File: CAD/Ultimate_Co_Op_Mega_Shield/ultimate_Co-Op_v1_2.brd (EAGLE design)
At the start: 78.4 x 53.3 mm, 134 parts

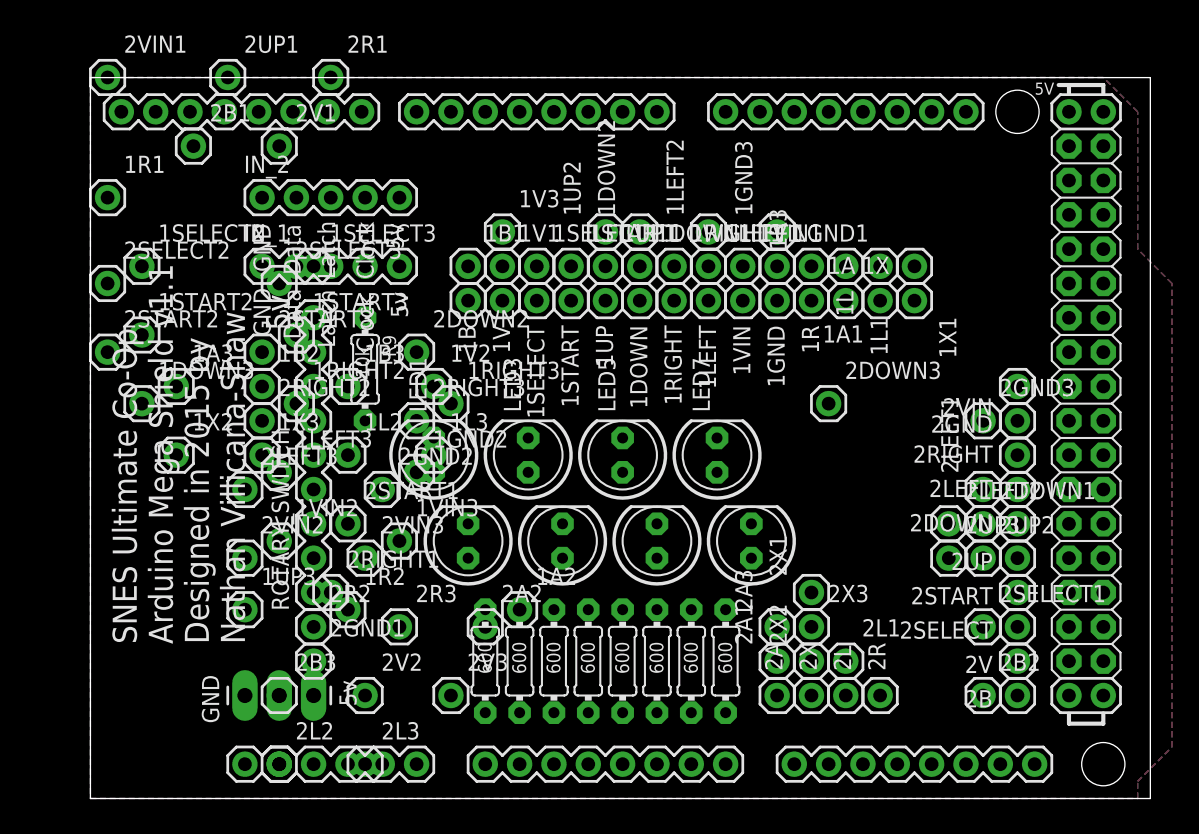
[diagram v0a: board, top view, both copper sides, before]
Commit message: a few minor changes to the board, now has one rotaty and one switch
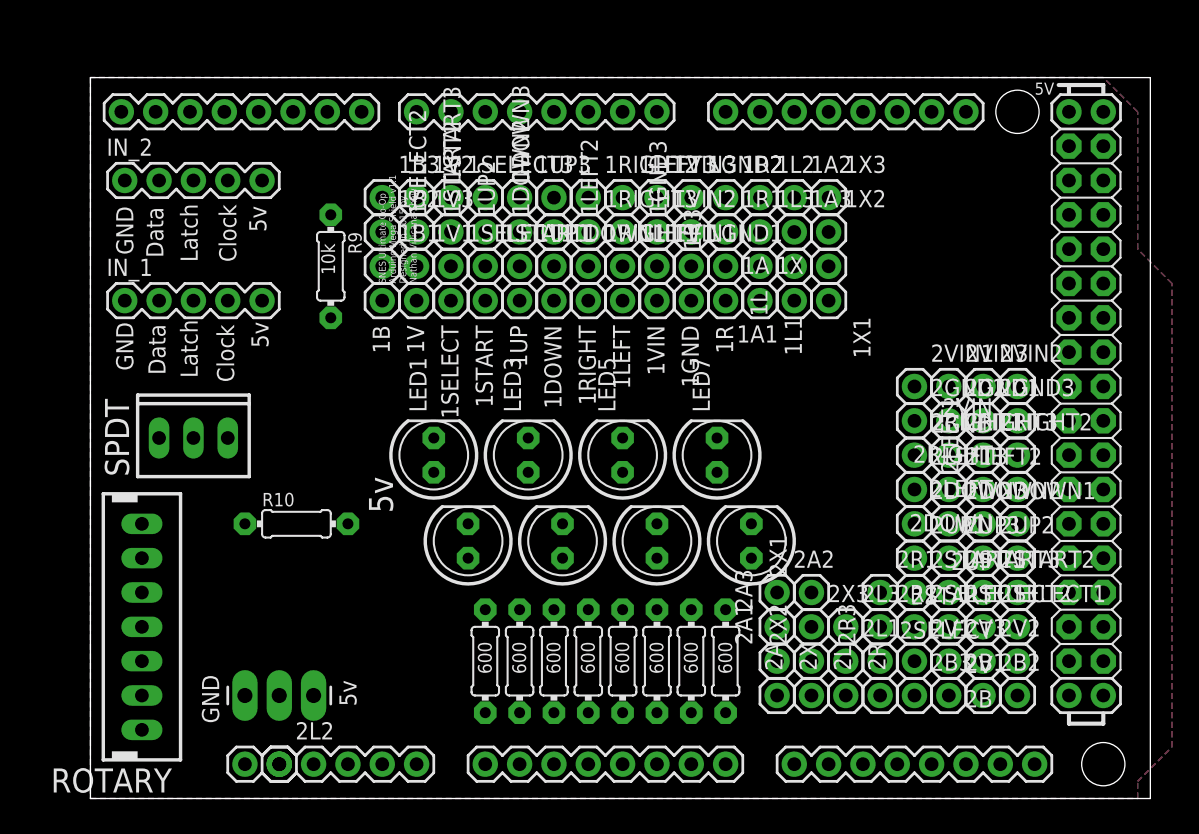
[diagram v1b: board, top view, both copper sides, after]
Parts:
- removed ROTARY_SWITCH: (no value), SparkFun-Connectors:1X09
- added R10: 10k, adafruit:0204/7
- added ROTARY: (no value), con-hdrs40:MTE-100-7V
- added SPDT: (no value), con-hdrs40:MTA-100-3V
- moved 2B1 69.1 mm to (63.5, 7.62)
- moved 2SELECT2 67.2 mm to (63.5, 12.7)
- moved 2START2 67.2 mm to (66.0, 15.2)
- moved 2VIN1 63.9 mm to (61.0, 30.5)
- moved 2UP1 62.0 mm to (61.0, 17.8)
- moved 2V1 60.5 mm to (61.0, 10.2)
- moved 2VIN2 56.1 mm to (66.0, 30.5)
- moved 2R1 55.7 mm to (58.4, 15.2)
- moved 2START3 53.8 mm to (63.5, 15.2)
- moved 2SELECT3 53.4 mm to (61.0, 12.7)
- moved 2RIGHT2 53.4 mm to (66.0, 25.4)
- moved 1X2 51.0 mm to (54.6, 41.9)
- moved 2GND1 50.2 mm to (63.5, 27.9)
- moved 2LEFT3 49.5 mm to (61.0, 22.9)
- moved 1A3 47.1 mm to (52.1, 41.9)
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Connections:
- new net OIJNENLK1: R10.1, ROTARY.7
- net 5V: now also R10.2
- net OIJNENLK: now also SPDT.3; no longer ROTARY_SWITCH.9
- net ROTARY_1: now also ROTARY.1; no longer ROTARY_SWITCH.1
- net ROTARY_2: now also ROTARY.2; no longer ROTARY_SWITCH.2
- net ROTARY_3: now also ROTARY.3; no longer ROTARY_SWITCH.3
- net ROTARY_4: now also ROTARY.4; no longer ROTARY_SWITCH.4
- net ROTARY_5: now also ROTARY.5; no longer ROTARY_SWITCH.5
- net ROTARY_6: now also ROTARY.6; no longer ROTARY_SWITCH.6
- net ROTARY_7: now also SPDT.1; no longer ROTARY_SWITCH.7
- net ROTARY_8: now also SPDT.2; no longer ROTARY_SWITCH.8
